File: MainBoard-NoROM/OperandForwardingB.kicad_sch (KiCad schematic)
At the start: 6 parts, among them U47 74AHCT16245, U48 74AHCT16245, U49 74AHCT16245

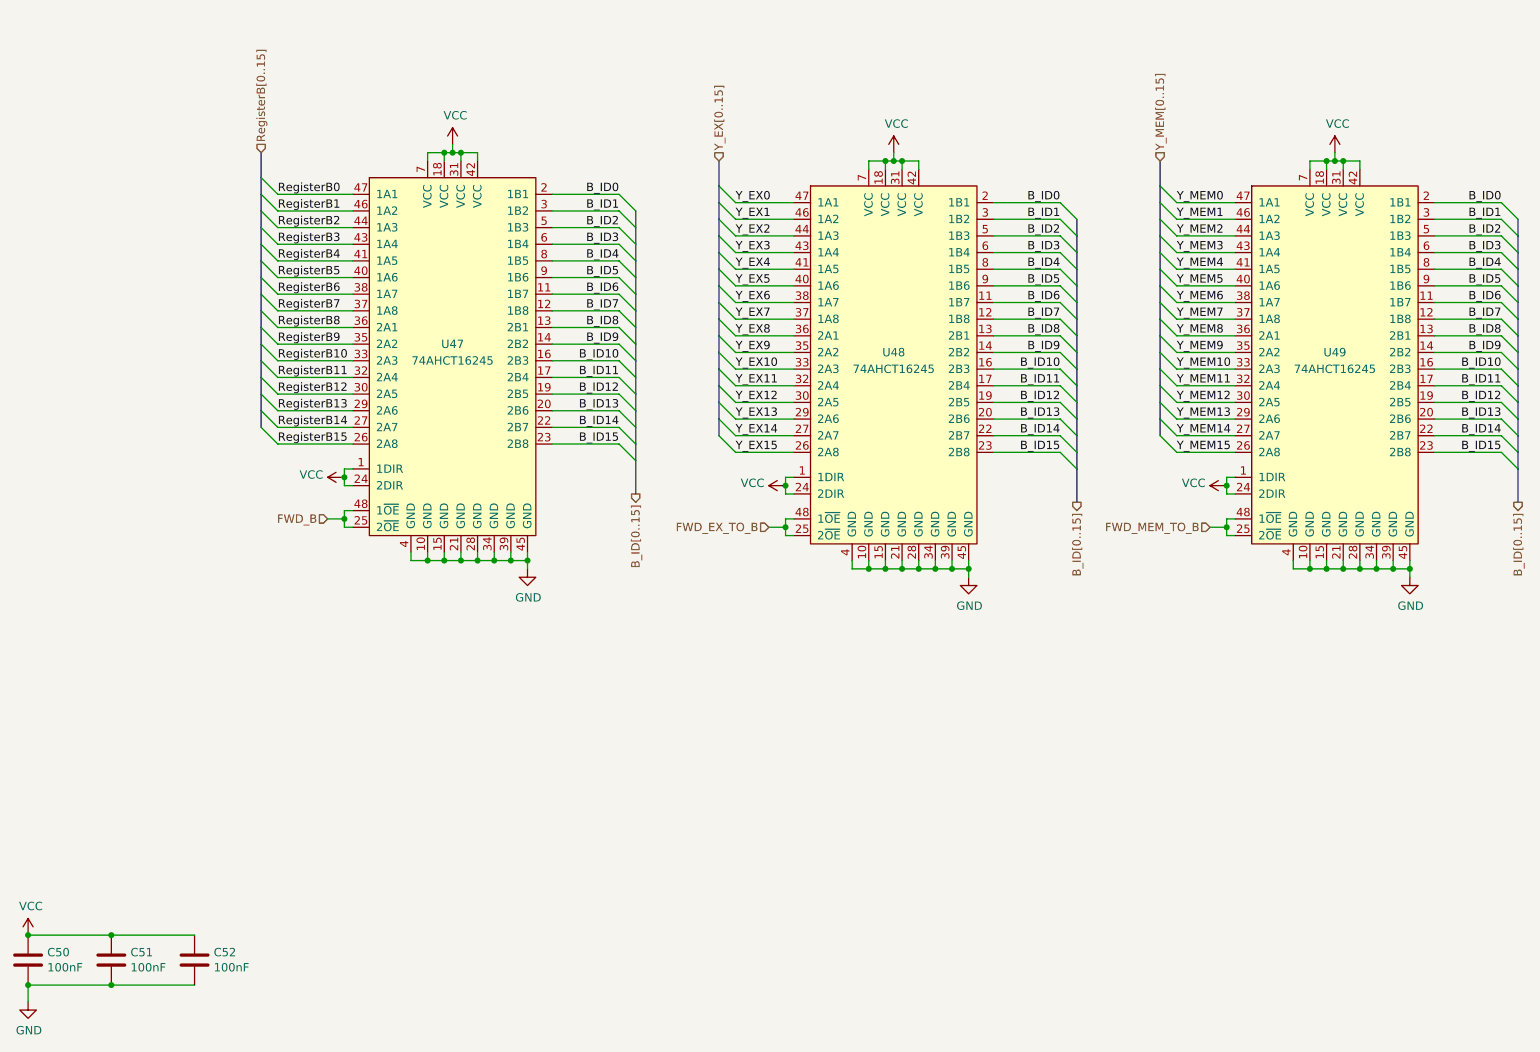
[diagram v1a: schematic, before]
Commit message: Update schematics for the MainBoard to include the ControleModule fix from 704c0dce
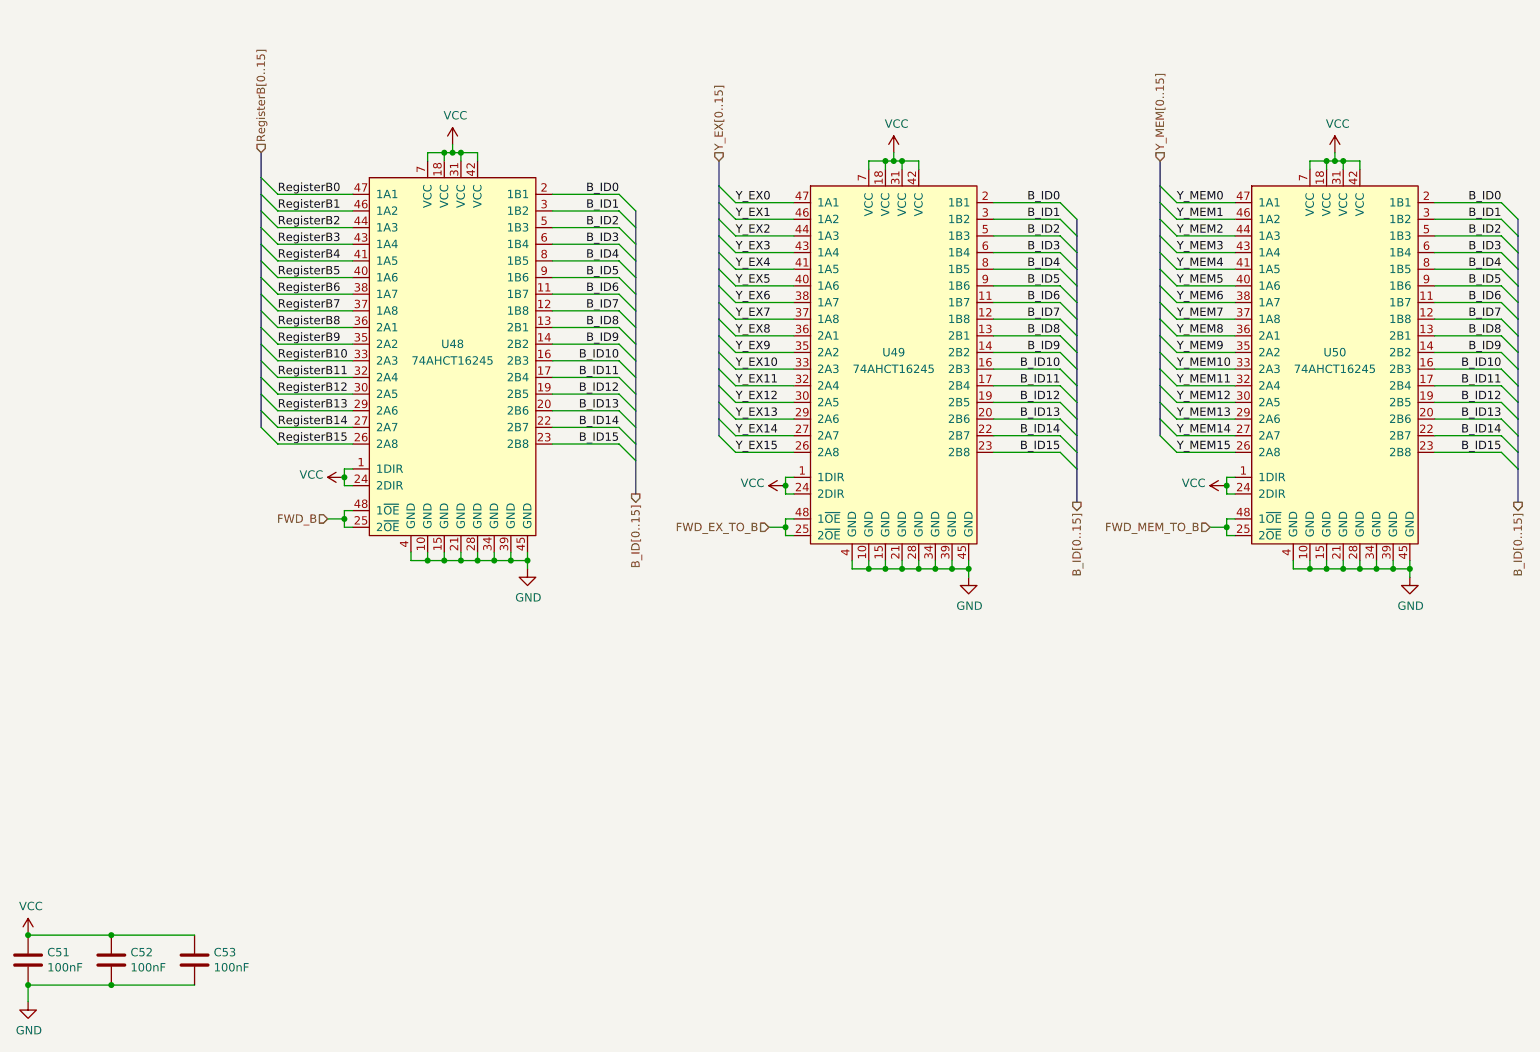
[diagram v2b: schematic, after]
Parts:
- renumbered C50 to C51, C51 to C52, C52 to C53, U47 to U48, U48 to U49, U49 to U50
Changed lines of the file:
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@@
   (symbol (lib_id "Device:C") (at 31.75 185.42 0) (unit 1)
     (in_bom yes) (on_board yes) (dnp no)
-    (property "Reference" "C51" (at 34.671 184.2516 0)
+    (property "Reference" "C52" (at 34.671 184.2516 0)
       (effects (font (size 1.27 1.27)) (justify left))
     )
@@
       (project "MainBoard"
         (path "/83c5181e-f5ee-453c-ae5c-d7256ba8837d/2e370670-2291-4657-8360-03c3bd44e418"
-          (reference "C51") (unit 1)
+          (reference "C52") (unit 1)
         )
       )
@@
   (symbol (lib_id "power:VCC") (at 19.05 181.61 0) (unit 1)
     (in_bom yes) (on_board yes) (dnp no)
-    (property "Reference" "#PWR0268" (at 19.05 185.42 0)
+    (property "Reference" "#PWR0270" (at 19.05 185.42 0)
       (effects (font (size 1.27 1.27)) hide)
     )
@@
       (project "MainBoard"
         (path "/83c5181e-f5ee-453c-ae5c-d7256ba8837d/2e370670-2291-4657-8360-03c3bd44e418"
-          (reference "#PWR0268") (unit 1)
+          (reference "#PWR0270") (unit 1)
         )
       )
@@
   (symbol (lib_id "power:GND") (at 19.05 191.77 0) (unit 1)
     (in_bom yes) (on_board yes) (dnp no)
-    (property "Reference" "#PWR0269" (at 19.05 198.12 0)
+    (property "Reference" "#PWR0271" (at 19.05 198.12 0)
       (effects (font (size 1.27 1.27)) hide)
     )
@@
       (project "MainBoard"
         (path "/83c5181e-f5ee-453c-ae5c-d7256ba8837d/2e370670-2291-4657-8360-03c3bd44e418"
-          (reference "#PWR0269") (unit 1)
+          (reference "#PWR0271") (unit 1)
         )
       )
@@
   (symbol (lib_id "Device:C") (at 44.45 185.42 0) (unit 1)
     (in_bom yes) (on_board yes) (dnp no)
-    (property "Reference" "C52" (at 47.371 184.2516 0)
+    (property "Reference" "C53" (at 47.371 184.2516 0)
       (effects (font (size 1.27 1.27)) (justify left))
     )
@@
       (project "MainBoard"
         (path "/83c5181e-f5ee-453c-ae5c-d7256ba8837d/2e370670-2291-4657-8360-03c3bd44e418"
-          (reference "C52") (unit 1)
+          (reference "C53") (unit 1)
         )
       )
@@
   (symbol (lib_id "power:VCC") (at 83.82 60.96 0) (unit 1)
     (in_bom yes) (on_board yes) (dnp no)
-    (property "Reference" "#PWR0271" (at 83.82 64.77 0)
+    (property "Reference" "#PWR0273" (at 83.82 64.77 0)
       (effects (font (size 1.27 1.27)) hide)
     )
@@
       (project "MainBoard"
         (path "/83c5181e-f5ee-453c-ae5c-d7256ba8837d/2e370670-2291-4657-8360-03c3bd44e418"
-          (reference "#PWR0271") (unit 1)
+          (reference "#PWR0273") (unit 1)
         )
       )
@@
   (symbol (lib_id "power:GND") (at 95.25 125.73 0) (unit 1)
     (in_bom yes) (on_board yes) (dnp no)
-    (property "Reference" "#PWR0272" (at 95.25 132.08 0)
+    (property "Reference" "#PWR0274" (at 95.25 132.08 0)
       (effects (font (size 1.27 1.27)) hide)
     )
@@
       (project "MainBoard"
         (path "/83c5181e-f5ee-453c-ae5c-d7256ba8837d/2e370670-2291-4657-8360-03c3bd44e418"
-          (reference "#PWR0272") (unit 1)
+          (reference "#PWR0274") (unit 1)
         )
       )
@@
   (symbol (lib_id "74xx (kicad5):74AHCT16245") (at 83.82 92.71 0) (unit 1)
     (in_bom yes) (on_board yes) (dnp no)
-    (property "Reference" "U47" (at 83.82 91.44 0)
+    (property "Reference" "U48" (at 83.82 91.44 0)
       (effects (font (size 1.27 1.27)))
     )
@@
       (project "MainBoard"
         (path "/83c5181e-f5ee-453c-ae5c-d7256ba8837d/2e370670-2291-4657-8360-03c3bd44e418"
-          (reference "U47") (unit 1)
+          (reference "U48") (unit 1)
         )
       )
@@
   (symbol (lib_id "74xx (kicad5):74AHCT16245") (at 151.13 93.98 0) (unit 1)
     (in_bom yes) (on_board yes) (dnp no)
-    (property "Reference" "U48" (at 151.13 92.71 0)
+    (property "Reference" "U49" (at 151.13 92.71 0)
       (effects (font (size 1.27 1.27)))
     )
@@
       (project "MainBoard"
         (path "/83c5181e-f5ee-453c-ae5c-d7256ba8837d/2e370670-2291-4657-8360-03c3bd44e418"
-          (reference "U48") (unit 1)
+          (reference "U49") (unit 1)
         )
       )
@@
   (symbol (lib_id "power:VCC") (at 134.62 113.03 90) (unit 1)
     (in_bom yes) (on_board yes) (dnp no)
-    (property "Reference" "#PWR0273" (at 138.43 113.03 0)
+    (property "Reference" "#PWR0275" (at 138.43 113.03 0)
       (effects (font (size 1.27 1.27)) hide)
     )
@@
       (project "MainBoard"
         (path "/83c5181e-f5ee-453c-ae5c-d7256ba8837d/2e370670-2291-4657-8360-03c3bd44e418"
-          (reference "#PWR0273") (unit 1)
+          (reference "#PWR0275") (unit 1)
         )
       )
@@
   (symbol (lib_id "power:GND") (at 162.56 127 0) (unit 1)
     (in_bom yes) (on_board yes) (dnp no)
-    (property "Reference" "#PWR0275" (at 162.56 133.35 0)
+    (property "Reference" "#PWR0277" (at 162.56 133.35 0)
       (effects (font (size 1.27 1.27)) hide)
     )
@@
       (project "MainBoard"
         (path "/83c5181e-f5ee-453c-ae5c-d7256ba8837d/2e370670-2291-4657-8360-03c3bd44e418"
-          (reference "#PWR0275") (unit 1)
+          (reference "#PWR0277") (unit 1)
         )
       )
@@
   (symbol (lib_id "power:VCC") (at 151.13 62.23 0) (unit 1)
     (in_bom yes) (on_board yes) (dnp no)
-    (property "Reference" "#PWR0274" (at 151.13 66.04 0)
+    (property "Reference" "#PWR0276" (at 151.13 66.04 0)
       (effects (font (size 1.27 1.27)) hide)
     )
@@
       (project "MainBoard"
         (path "/83c5181e-f5ee-453c-ae5c-d7256ba8837d/2e370670-2291-4657-8360-03c3bd44e418"
-          (reference "#PWR0274") (unit 1)
+          (reference "#PWR0276") (unit 1)
         )
       )
@@
   (symbol (lib_id "74xx (kicad5):74AHCT16245") (at 218.44 93.98 0) (unit 1)
     (in_bom yes) (on_board yes) (dnp no)
-    (property "Reference" "U49" (at 218.44 92.71 0)
+    (property "Reference" "U50" (at 218.44 92.71 0)
       (effects (font (size 1.27 1.27)))
     )
@@
       (project "MainBoard"
         (path "/83c5181e-f5ee-453c-ae5c-d7256ba8837d/2e370670-2291-4657-8360-03c3bd44e418"
-          (reference "U49") (unit 1)
+          (reference "U50") (unit 1)
         )
       )
@@
   (symbol (lib_id "power:VCC") (at 201.93 113.03 90) (unit 1)
     (in_bom yes) (on_board yes) (dnp no)
-    (property "Reference" "#PWR0276" (at 205.74 113.03 0)
+    (property "Reference" "#PWR0278" (at 205.74 113.03 0)
       (effects (font (size 1.27 1.27)) hide)
     )
@@
       (project "MainBoard"
         (path "/83c5181e-f5ee-453c-ae5c-d7256ba8837d/2e370670-2291-4657-8360-03c3bd44e418"
-          (reference "#PWR0276") (unit 1)
+          (reference "#PWR0278") (unit 1)
         )
       )
@@
   (symbol (lib_id "Device:C") (at 19.05 185.42 0) (unit 1)
     (in_bom yes) (on_board yes) (dnp no)
-    (property "Reference" "C50" (at 21.971 184.2516 0)
+    (property "Reference" "C51" (at 21.971 184.2516 0)
       (effects (font (size 1.27 1.27)) (justify left))
     )
@@
       (project "MainBoard"
         (path "/83c5181e-f5ee-453c-ae5c-d7256ba8837d/2e370670-2291-4657-8360-03c3bd44e418"
-          (reference "C50") (unit 1)
+          (reference "C51") (unit 1)
         )
       )
@@
   (symbol (lib_id "power:VCC") (at 67.31 111.76 90) (unit 1)
     (in_bom yes) (on_board yes) (dnp no)
-    (property "Reference" "#PWR0270" (at 71.12 111.76 0)
+    (property "Reference" "#PWR0272" (at 71.12 111.76 0)
       (effects (font (size 1.27 1.27)) hide)
     )
@@
       (project "MainBoard"
         (path "/83c5181e-f5ee-453c-ae5c-d7256ba8837d/2e370670-2291-4657-8360-03c3bd44e418"
-          (reference "#PWR0270") (unit 1)
+          (reference "#PWR0272") (unit 1)
         )
       )
@@
   (symbol (lib_id "power:GND") (at 229.87 127 0) (unit 1)
     (in_bom yes) (on_board yes) (dnp no)
-    (property "Reference" "#PWR0278" (at 229.87 133.35 0)
+    (property "Reference" "#PWR0280" (at 229.87 133.35 0)
       (effects (font (size 1.27 1.27)) hide)
     )
@@
       (project "MainBoard"
         (path "/83c5181e-f5ee-453c-ae5c-d7256ba8837d/2e370670-2291-4657-8360-03c3bd44e418"
-          (reference "#PWR0278") (unit 1)
+          (reference "#PWR0280") (unit 1)
         )
       )
@@
   (symbol (lib_id "power:VCC") (at 218.44 62.23 0) (unit 1)
     (in_bom yes) (on_board yes) (dnp no)
-    (property "Reference" "#PWR0277" (at 218.44 66.04 0)
+    (property "Reference" "#PWR0279" (at 218.44 66.04 0)
       (effects (font (size 1.27 1.27)) hide)
     )
@@
       (project "MainBoard"
         (path "/83c5181e-f5ee-453c-ae5c-d7256ba8837d/2e370670-2291-4657-8360-03c3bd44e418"
-          (reference "#PWR0277") (unit 1)
-        )
-      )
+          (reference "#PWR0279") (unit 1)
+        )
+      )
